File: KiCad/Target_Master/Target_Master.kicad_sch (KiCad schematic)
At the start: 9 parts, among them J1 RJ11 Header, U2 PIC16F1788-IP

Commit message: Finalized schematics
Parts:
- added C12: 220uF, symbol Device:C_Polarized_Small_US
- added C13: 0.1uF, symbol Device:C_Small
- R3, R4: value 4.7kΩ -> 220Ω
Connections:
- net +5V: now also C12.1, C13.1
- net GND: now also C12.2, C13.2
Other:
- moved on the sheet: C4, D2, R2

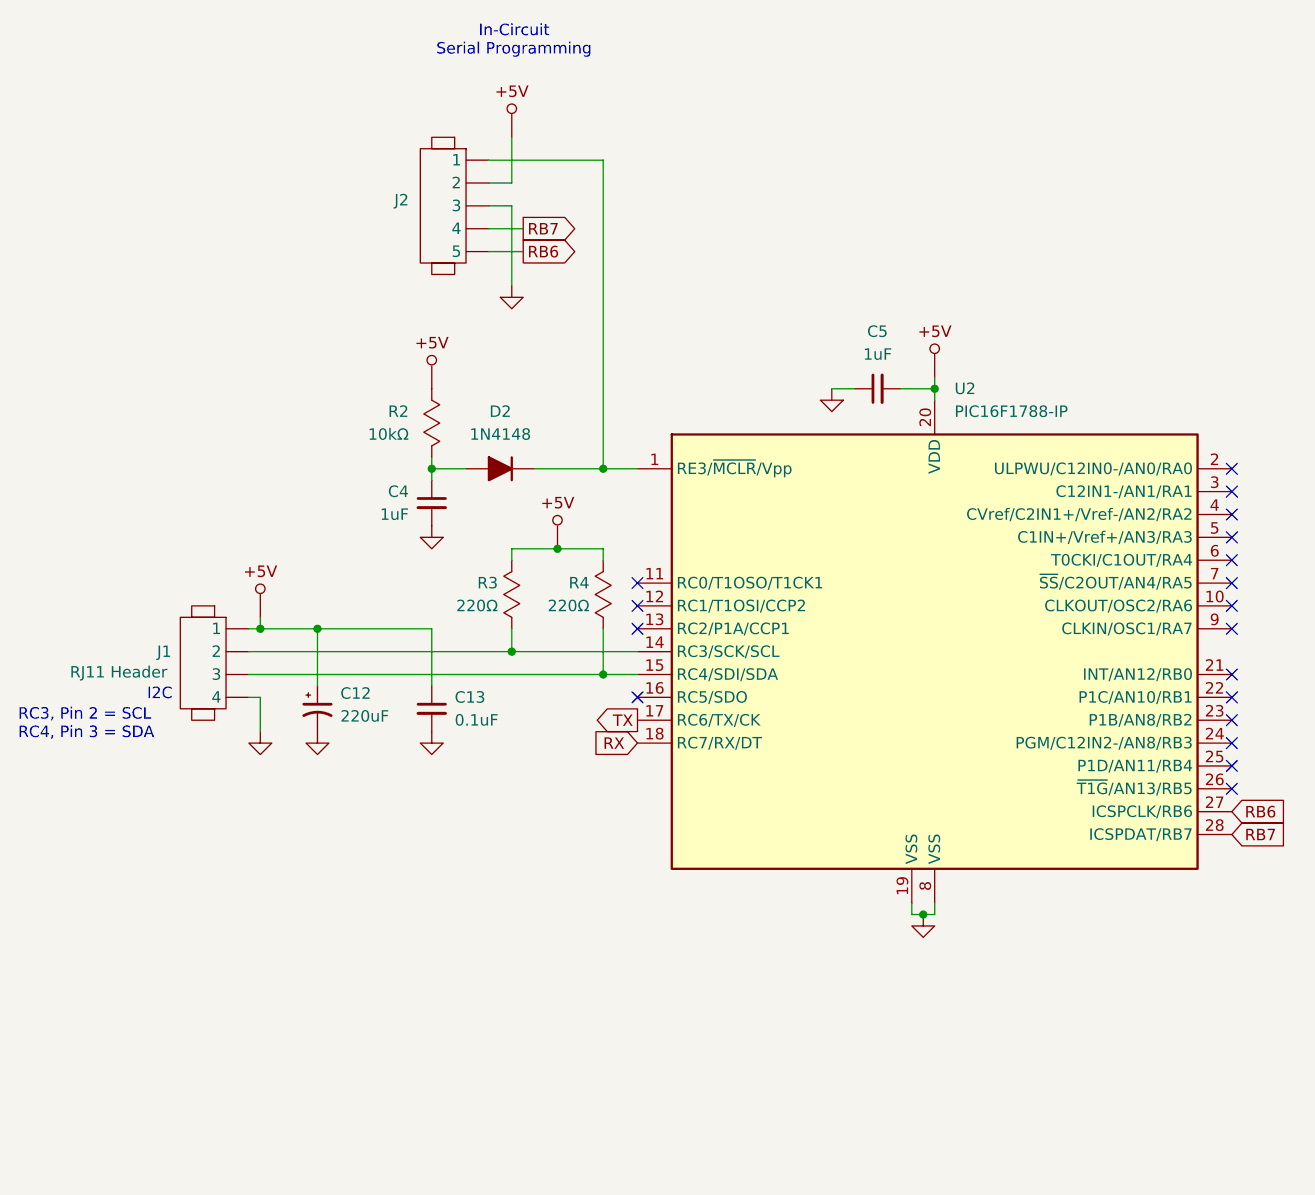
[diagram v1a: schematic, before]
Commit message: Master PCB design, Slave board logos
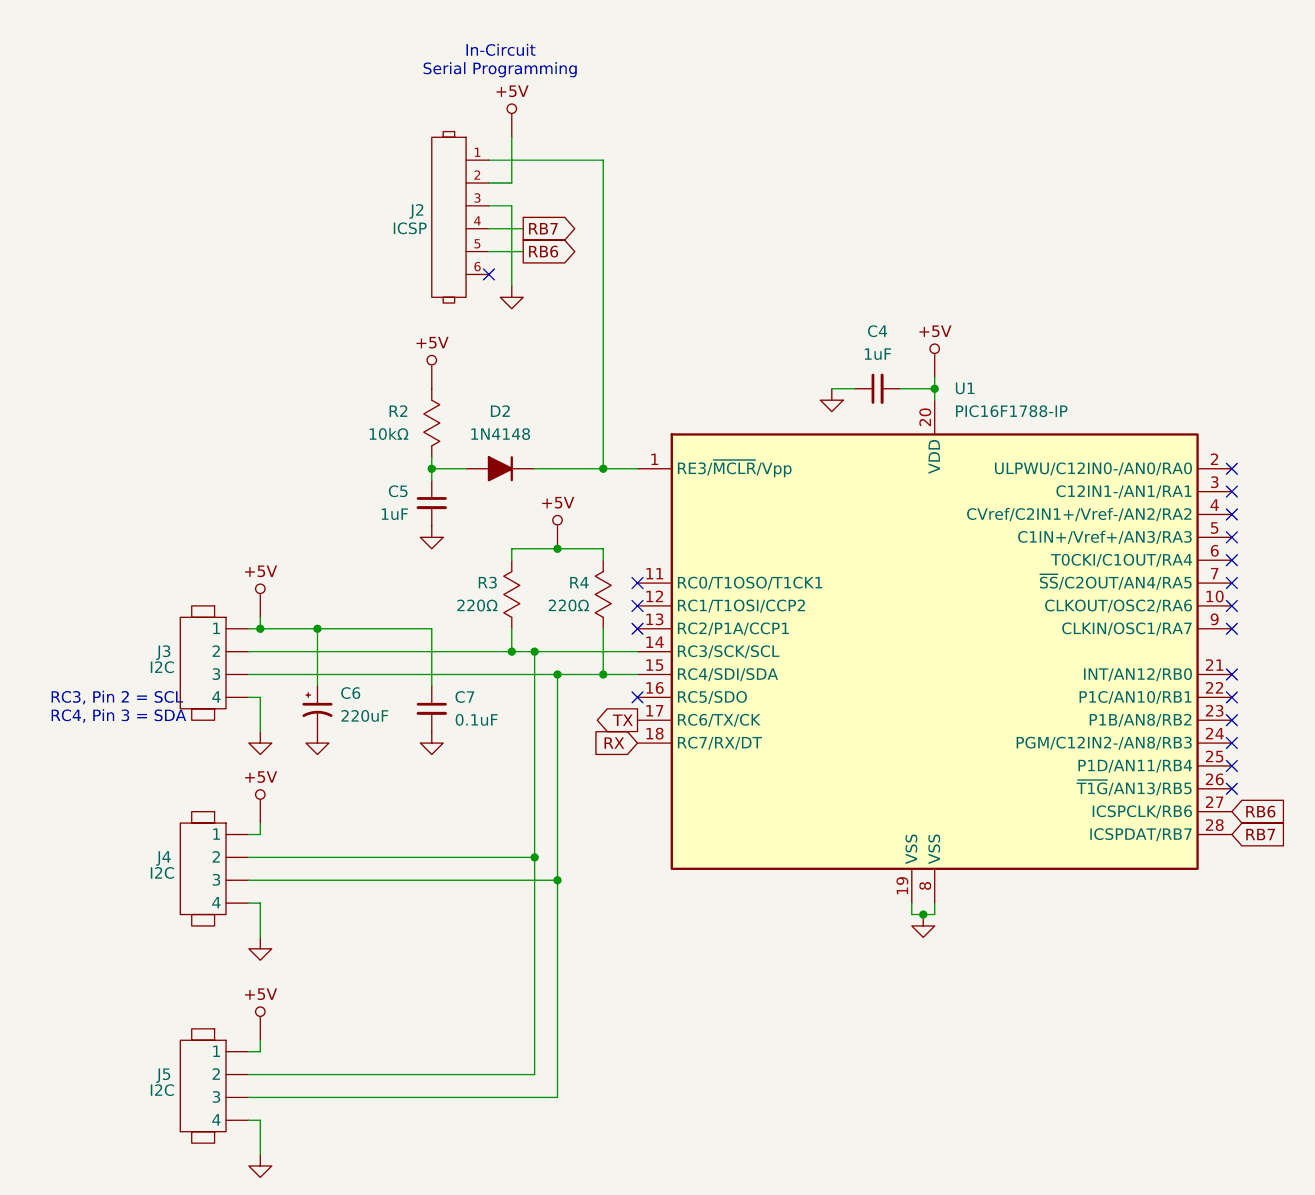
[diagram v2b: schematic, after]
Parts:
- removed J1: RJ11 Header, AlexWheelockFootprintLibrary:RJ11_Connector, symbol Libraries:Header_1x4
- removed J2: ~, Connector_PinHeader_2.54mm:PinHeader_1x05_P2.54mm_Vertical, symbol Libraries:Header_1x5
- added J2: ICSP, 0_AKeller_Footprints:1x6_100mil_Header, symbol 0_AKeller_Parts:Header_1x6
- added J3, J4, J5: I2C, 0_AKeller_Footprints:1x4_100mil_Header, symbol Libraries:Header_1x4
- C6: renamed from C12; footprint (none) -> Capacitor_THT:CP_Radial_D6.3mm_P2.50mm
- C7: renamed from C13; footprint (none) -> Capacitor_SMD:C_0805_2012Metric_Pad1.18x1.45mm_HandSolder
- D2: footprint Diode_SMD:D_0805_2012Metric_Pad1.15x1.40mm_HandSolder -> 0_AKeller_Footprints:Diode_0805
- U1: renamed from U2; footprint (none) -> 0_AKeller_Footprints:SSOP-28
- renumbered C5 to C4, C4 to C5
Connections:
- net +5V: now also J2.2, J3.1, J4.1, J5.1
- net GND: now also J2.3, J3.4, J4.4, J5.4
- net RB6: now also J2.5
- net RB7: now also J2.4
- net at D2.1 (K), U1.1 (RE3/~{MCLR}/Vpp): now also J2.1
- net at R3.2, U1.14 (RC3/SCK/SCL): now also J3.2, J4.2, J5.2
- net at R4.2, U1.15 (RC4/SDI/SDA): now also J3.3, J4.3, J5.3
- no-connect marks 18 -> 19
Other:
- note removed: "I2C"

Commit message: Master board silkscreen and gerber files
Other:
- title: Master -> Laser Arcade Master
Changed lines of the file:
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@@
 	(paper "A")
 	(title_block
-		(title "Master")
-		(date "2025-04-04")
+		(title "Laser Arcade Master")
+		(date "2025-04-17")
 		(rev "A")
 		(company "Idaho State University")
